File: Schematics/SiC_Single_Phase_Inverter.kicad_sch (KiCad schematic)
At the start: 8 parts, among them J1 23AH8786-Red, J2 23AH8785-Black, J3 23AH8786-Red, J4 23AH8785-Black

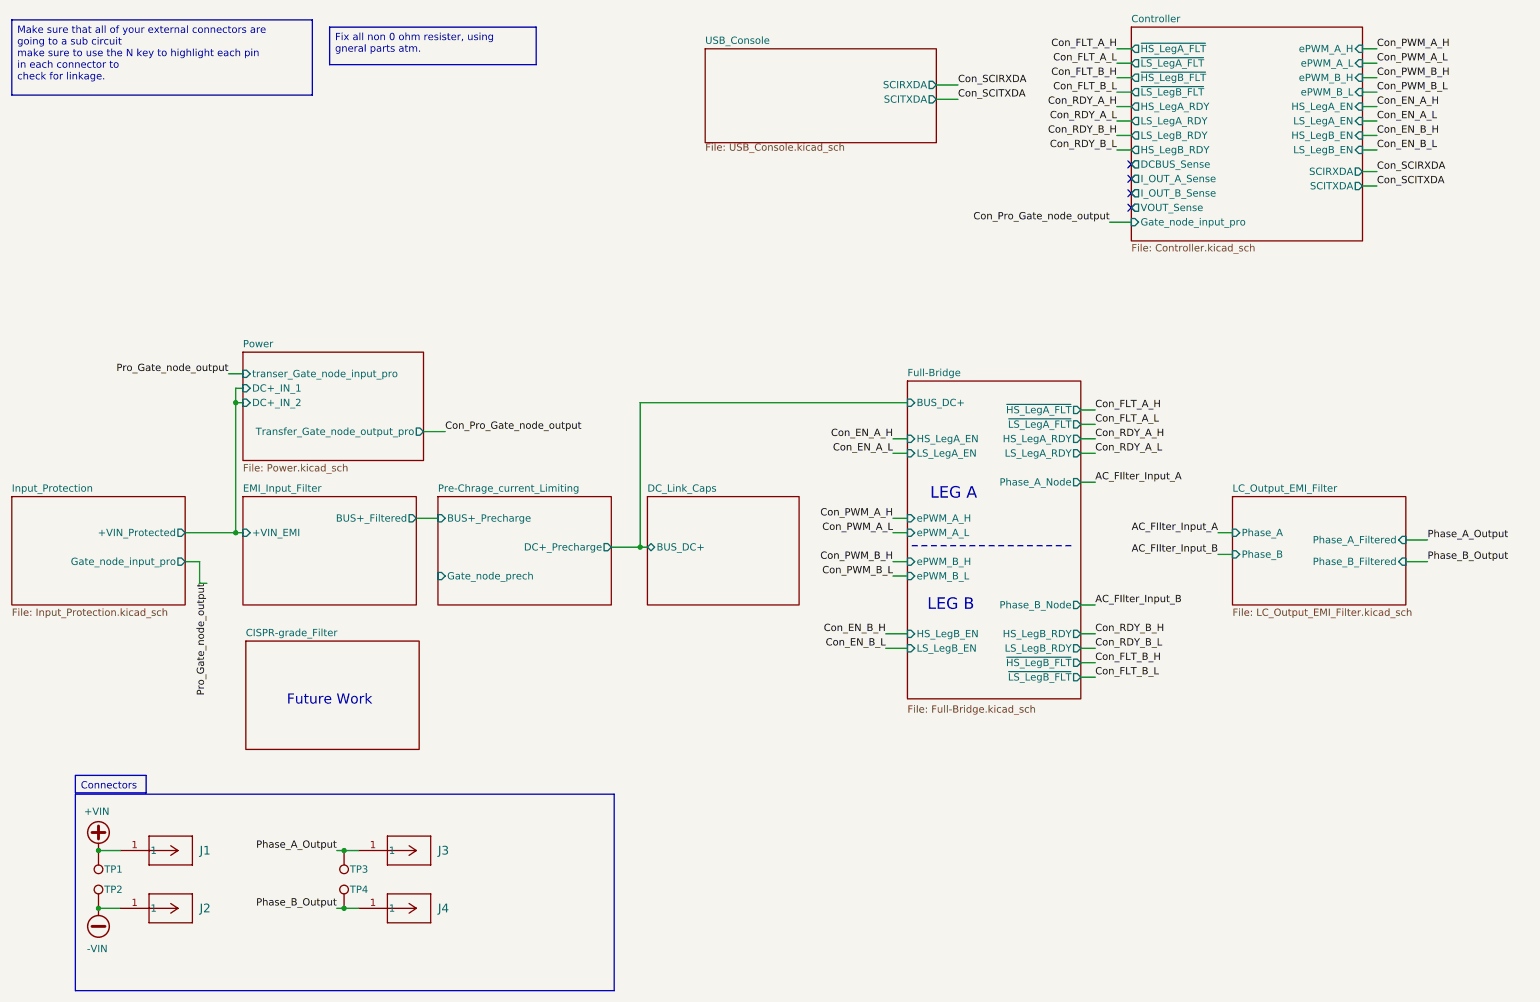
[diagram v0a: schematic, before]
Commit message: Added Precharge Gate Driver to controller and per charge sub circuit
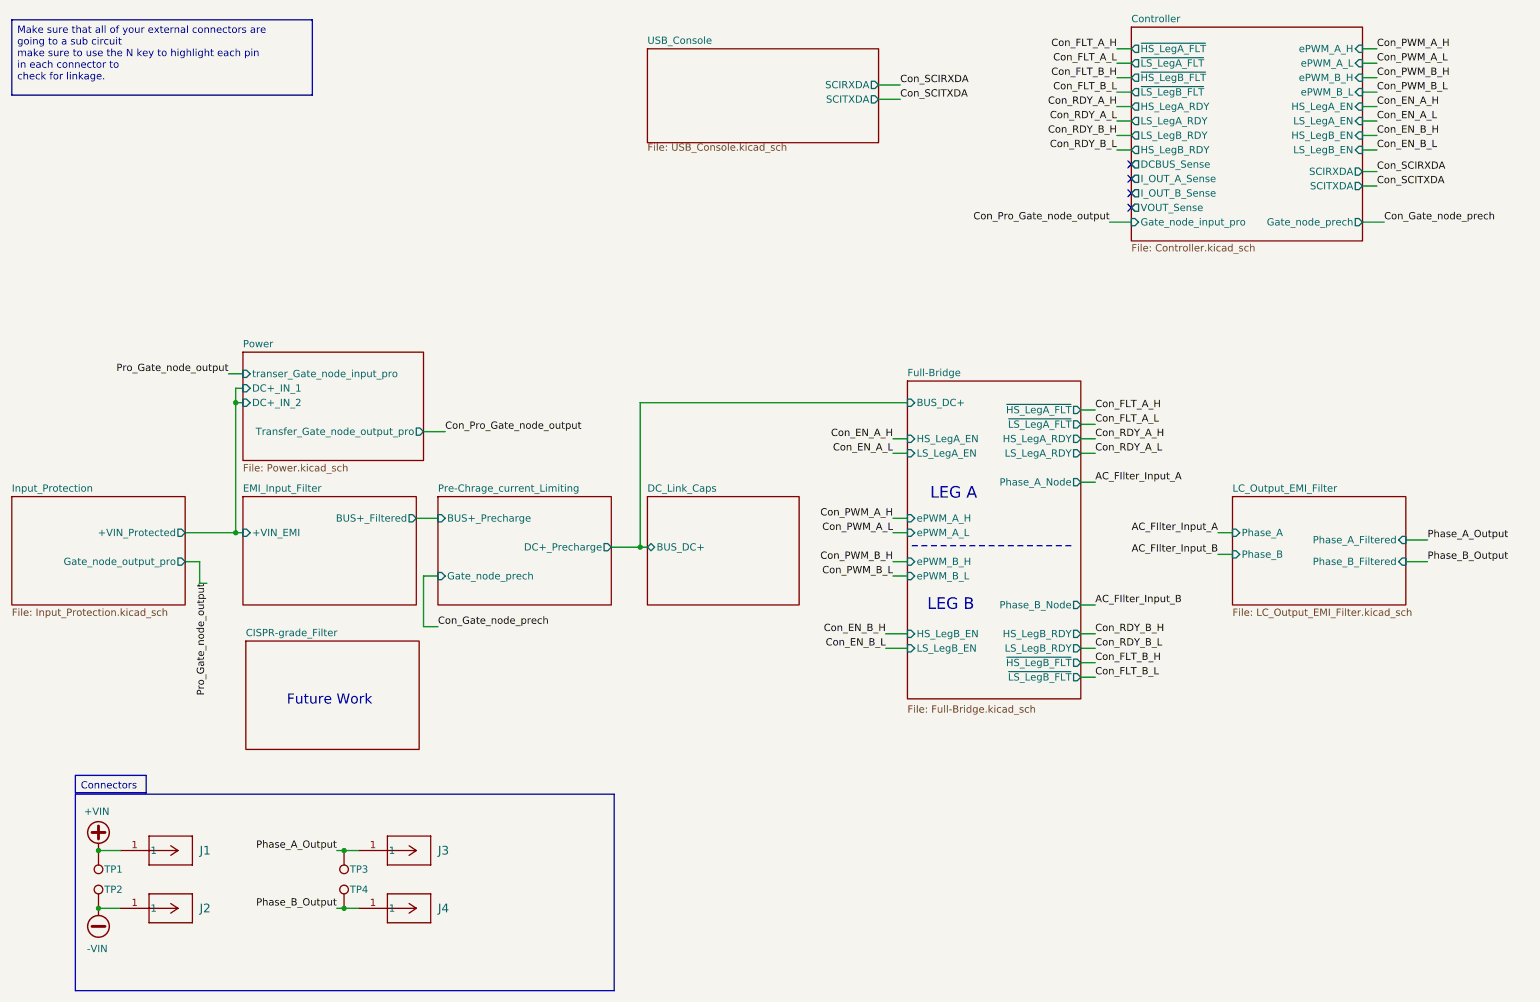
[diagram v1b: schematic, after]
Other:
- sheet Controller ports: added Gate_node_prech; removed none
- sheet Input_Protection ports: added Gate_node_output_pro; removed Gate_node_input_pro
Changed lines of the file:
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@@
-		)
-	)
-	(text_box "Fix all non 0 ohm resister, using gneral parts atm. "
-		(exclude_from_sim no)
-		(at 71.12 17.78 0)
-		(size 36.322 6.604)
-		(margins 0.9525 0.9525 0.9525 0.9525)
-		(stroke
-			(width 0)
-			(type solid)
-		)
-		(fill
-			(type color)
-			(color 0 0 255 0.1)
-		)
-		(effects
-			(font
-				(size 1.27 1.27)
-			)
-			(justify left top)
 		)
 	)
@@
 		)
 	)
+	(wire
+		(pts
+			(xy 252.73 52.07) (xy 256.54 52.07)
+		)
+		(stroke
+			(width 0)
+			(type default)
+		)
+	)
 	(polyline
 		(pts
@@
 	(wire
 		(pts
+			(xy 87.63 114.3) (xy 90.17 114.3)
+		)
+		(stroke
+			(width 0)
+			(type default)
+		)
+	)
+	(wire
+		(pts
 			(xy 203.2 92.71) (xy 205.74 92.71)
 		)
@@
 	(wire
 		(pts
-			(xy 177.8 30.48) (xy 181.61 30.48)
+			(xy 167.64 30.48) (xy 171.45 30.48)
 		)
 		(stroke
@@
 	(wire
 		(pts
-			(xy 177.8 27.94) (xy 181.61 27.94)
+			(xy 167.64 27.94) (xy 171.45 27.94)
 		)
 		(stroke
@@
 	(wire
 		(pts
+			(xy 87.63 123.19) (xy 87.63 114.3)
+		)
+		(stroke
+			(width 0)
+			(type default)
+		)
+	)
+	(wire
+		(pts
 			(xy 209.55 29.21) (xy 212.09 29.21)
 		)
@@
 		(pts
 			(xy 170.18 106.68) (xy 172.72 106.68)
+		)
+		(stroke
+			(width 0)
+			(type default)
+		)
+	)
+	(wire
+		(pts
+			(xy 90.17 123.19) (xy 87.63 123.19)
 		)
 		(stroke
@@
 		)
 	)
+	(label "Con_Gate_node_prech"
+		(at 90.17 123.19 0)
+		(effects
+			(font
+				(size 1.27 1.27)
+			)
+			(justify left bottom)
+		)
+	)
 	(label "Con_SCIRXDA"
-		(at 181.61 27.94 0)
+		(at 171.45 27.94 0)
 		(effects
 			(font
@@
 		)
 	)
+	(label "Con_Gate_node_prech"
+		(at 256.54 52.07 0)
+		(effects
+			(font
+				(size 1.27 1.27)
+			)
+			(justify left bottom)
+		)
+	)
 	(label "Phase_B_Output"
 		(at 264.16 111.76 0)
@@
 	)
 	(label "Con_SCITXDA"
-		(at 181.61 30.48 0)
+		(at 171.45 30.48 0)
 		(effects
 			(font
@@
 			)
 		)
+		(pin "Gate_node_prech" output
+			(at 252.73 52.07 0)
+			(effects
+				(font
+					(size 1.27 1.27)
+				)
+				(justify right)
+			)
+		)
 		(instances
 			(project "SiC_Single_Phase_Inverter"
@@
 	)
 	(sheet
-		(at 137.16 21.59)
+		(at 127 21.59)
 		(size 40.64 16.51)
 		(exclude_from_sim no)
@@
 		)
 		(property "Sheetname" "USB_Console"
-			(at 137.16 20.8784 0)
+			(at 127 20.8784 0)
 			(effects
 				(font
@@
 		)
 		(property "Sheetfile" "USB_Console.kicad_sch"
-			(at 137.16 38.1766 0)
+			(at 127 38.1766 0)
 			(effects
 				(font
@@
 		)
 		(pin "SCIRXDA" output
-			(at 177.8 27.94 0)
+			(at 167.64 27.94 0)
 			(effects
 				(font
@@
 		)
 		(pin "SCITXDA" output
-			(at 177.8 30.48 0)
+			(at 167.64 30.48 0)
 			(effects
 				(font
@@
 			)
 		)
-		(pin "Gate_node_input_pro" output
+		(pin "Gate_node_output_pro" output
 			(at 45.72 111.76 0)
 			(effects

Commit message: WIP PCB, Added Test Points, added icon file
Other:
- sheet Pre-Chrage_current_Limiting renamed Pre-charge_current_Limiting
- moved on the sheet: J3, J4, TP1, TP4
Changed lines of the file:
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@@
-	)
-	(junction
-		(at 73.66 162.56)
-		(diameter 0)
-		(color 0 0 0 0)
 	)
 	(junction
@@
 	)
 	(junction
-		(at 73.66 172.72)
+		(at 73.66 173.99)
 		(diameter 0)
 		(color 0 0 0 0)
@@
 		(color 0 0 0 0)
 	)
+	(junction
+		(at 73.66 163.83)
+		(diameter 0)
+		(color 0 0 0 0)
+	)
 	(no_connect
 		(at 212.09 44.45)
@@
 	(wire
 		(pts
+			(xy 73.66 163.83) (xy 76.2 163.83)
+		)
+		(stroke
+			(width 0)
+			(type default)
+		)
+	)
+	(wire
+		(pts
 			(xy 87.63 114.3) (xy 90.17 114.3)
 		)
@@
 	(wire
 		(pts
-			(xy 73.66 172.72) (xy 72.39 172.72)
+			(xy 73.66 173.99) (xy 72.39 173.99)
 		)
 		(stroke
@@
 	(wire
 		(pts
-			(xy 73.66 162.56) (xy 72.39 162.56)
+			(xy 72.39 163.83) (xy 73.66 163.83)
 		)
 		(stroke
@@
 	(wire
 		(pts
-			(xy 76.2 172.72) (xy 73.66 172.72)
+			(xy 76.2 173.99) (xy 73.66 173.99)
 		)
 		(stroke
@@
 		(pts
 			(xy 168.91 124.46) (xy 172.72 124.46)
-		)
-		(stroke
-			(width 0)
-			(type default)
-		)
-	)
-	(wire
-		(pts
-			(xy 76.2 162.56) (xy 73.66 162.56)
 		)
 		(stroke
@@
 	)
 	(label "Phase_A_Output"
-		(at 72.39 162.56 180)
+		(at 72.39 163.83 180)
 		(effects
 			(font
@@
 	)
 	(label "Phase_B_Output"
-		(at 72.39 172.72 180)
+		(at 72.39 173.99 180)
 		(effects
 			(font
@@
 	(symbol
 		(lib_id "SiC_Inverter:23AH8785-Black")
-		(at 76.2 172.72 0)
+		(at 76.2 173.99 0)
 		(unit 1)
 		(exclude_from_sim no)
@@
 		(fields_autoplaced yes)
 		(property "Reference" "J4"
-			(at 90.17 172.7199 0)
+			(at 90.17 173.9899 0)
 			(effects
 				(font
@@
 		)
 		(property "Value" "23AH8785-Black"
-			(at 88.392 181.61 0)
+			(at 88.392 182.88 0)
 			(effects
 				(font
@@
 		)
 		(property "Footprint" "SiC_Inverter:23AH8785-Black"
-			(at 92.456 177.546 0)
+			(at 92.456 178.816 0)
 			(effects
 				(font
@@
 		)
 		(property "Datasheet" "https://www.farnell.com/datasheets/3945771.pdf"
-			(at 105.41 179.578 0)
+			(at 105.41 180.848 0)
 			(effects
 				(font
@@
 		)
 		(property "Description" "Black:The 66.9040-22 is an 4mm Angled Socket for mounting on PCBs, gold-plated brass contact terminal."
-			(at 131.826 183.642 0)
+			(at 131.826 184.912 0)
 			(effects
 				(font
@@
 	(symbol
 		(lib_id "SiC_Inverter:5281")
-		(at 73.66 172.72 0)
+		(at 73.66 173.99 0)
 		(unit 1)
 		(exclude_from_sim no)
@@
 		(dnp no)
 		(property "Reference" "TP4"
-			(at 74.676 169.418 0)
+			(at 74.676 170.688 0)
 			(effects
 				(font
@@
 		)
 		(property "Value" "5281"
-			(at 57.658 185.674 0)
+			(at 57.658 186.944 0)
 			(effects
 				(font
@@
 		)
 		(property "Footprint" "SiC_Inverter:5281"
-			(at 63.754 183.896 0)
+			(at 63.754 185.166 0)
 			(effects
 				(font
@@
 		)
 		(property "Datasheet" "https://www.keyelco.com/userAssets/file/K75p62.pdf"
-			(at 81.534 180.086 0)
+			(at 81.534 181.356 0)
 			(effects
 				(font
@@
 		)
 		(property "Description" "Test Plugs & Test Jacks TEST POINT BLACK MULTIPURPOSE"
-			(at 84.074 182.118 0)
+			(at 84.074 183.388 0)
 			(effects
 				(font
@@
 	(symbol
 		(lib_id "SiC_Inverter:23AH8786-Red")
-		(at 76.2 162.56 0)
+		(at 76.2 163.83 0)
 		(unit 1)
 		(exclude_from_sim no)
@@
 		(fields_autoplaced yes)
 		(property "Reference" "J3"
-			(at 90.17 162.5599 0)
+			(at 90.17 163.8299 0)
 			(effects
 				(font
@@
 		)
 		(property "Value" "23AH8786-Red"
-			(at 87.884 171.45 0)
+			(at 87.884 172.72 0)
 			(effects
 				(font
@@
 		)
 		(property "Footprint" "SiC_Inverter:23AH8786-Red"
-			(at 93.726 167.386 0)
+			(at 93.726 168.656 0)
 			(effects
 				(font
@@
 		)
 		(property "Datasheet" "https://www.farnell.com/datasheets/3945771.pdf"
-			(at 106.172 169.418 0)
+			(at 106.172 170.688 0)
 			(effects
 				(font
@@
 		)
 		(property "Description" "Red: The 66.9040-22 is an 4mm Angled Socket for mounting on PCBs, gold-plated brass contact terminal."
-			(at 134.874 173.482 0)
+			(at 134.874 174.752 0)
 			(effects
 				(font
@@
 	(symbol
 		(lib_id "SiC_Inverter:5277")
-		(at 30.48 162.56 180)
+		(at 30.48 161.29 180)
 		(unit 1)
 		(exclude_from_sim no)
@@
 		(dnp no)
 		(property "Reference" "TP1"
-			(at 31.496 165.862 0)
+			(at 31.496 164.592 0)
 			(effects
 				(font
@@
 		)
 		(property "Value" "5277"
-			(at 46.482 149.606 0)
+			(at 46.482 148.336 0)
 			(effects
 				(font
@@
 		)
 		(property "Footprint" "SiC_Inverter:5277"
-			(at 40.386 151.384 0)
+			(at 40.386 150.114 0)
 			(effects
 				(font
@@
 		)
 		(property "Datasheet" "https://www.keyelco.com/userAssets/file/K75p62.pdf"
-			(at 22.606 155.194 0)
+			(at 22.606 153.924 0)
 			(effects
 				(font
@@
 		)
 		(property "Description" "Test Plugs & Test Jacks TEST POINT (BLUE) - COMPACT"
-			(at 20.066 153.162 0)
+			(at 20.066 151.892 0)
 			(effects
 				(font
@@
 			(color 0 0 0 0.0000)
 		)
-		(property "Sheetname" "Pre-Chrage_current_Limiting"
+		(property "Sheetname" "Pre-charge_current_Limiting"
 			(at 90.17 99.6184 0)
 			(effects

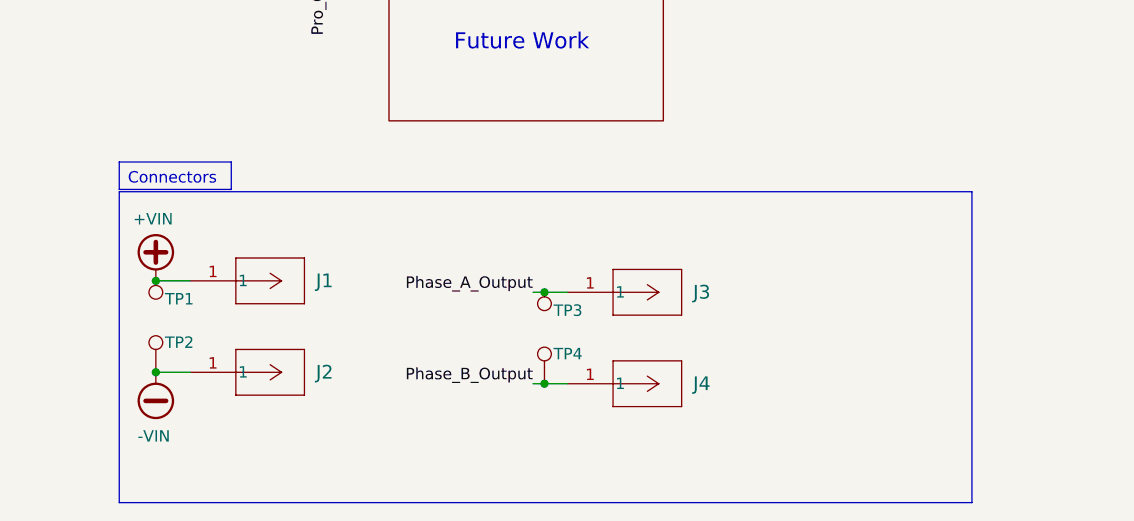
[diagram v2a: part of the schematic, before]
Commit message: WIP PCB Design: Finished DC Input / Protection Circuit
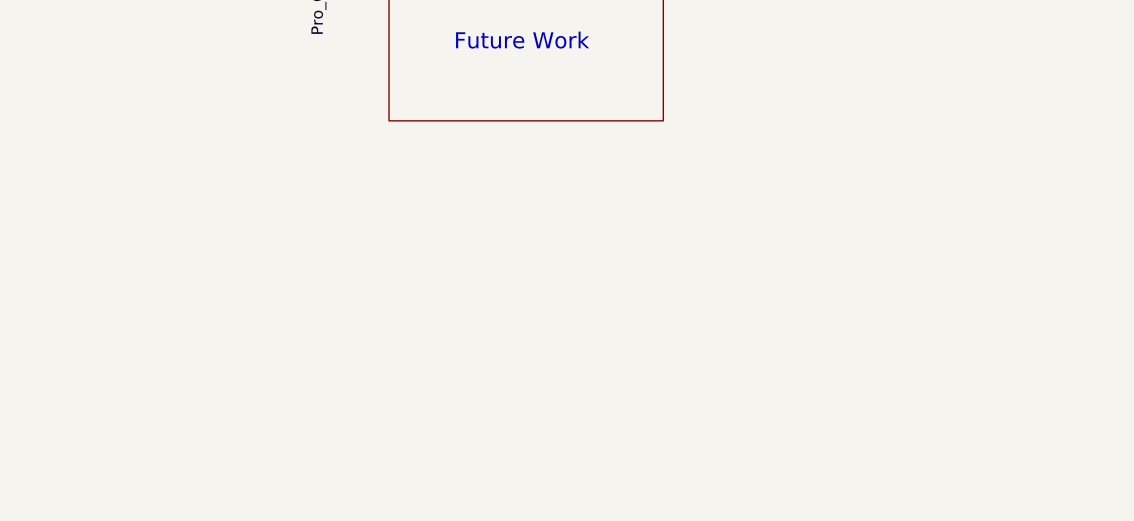
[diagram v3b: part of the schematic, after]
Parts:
- removed J1, J3: 23AH8786-Red, SiC_Inverter:23AH8786-Red, symbol SiC_Inverter:23AH8786-Red
- removed J2, J4: 23AH8785-Black, SiC_Inverter:23AH8785-Black, symbol SiC_Inverter:23AH8785-Black
- removed TP1, TP3: 5277, SiC_Inverter:5277, symbol SiC_Inverter:5277
- removed TP2, TP4: 5281, SiC_Inverter:5281, symbol SiC_Inverter:5281
